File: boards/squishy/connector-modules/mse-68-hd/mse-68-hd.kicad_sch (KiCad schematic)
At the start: 14 parts, among them J1 SCSI PHY Mezz, J2 Conn_02x25_Odd_Even, J3 Conn_01x04, J4 Conn_02x34_Clockwise_Shield, J5 Conn_02x24_Clockwise_Shield, U1 M24C02-RMC

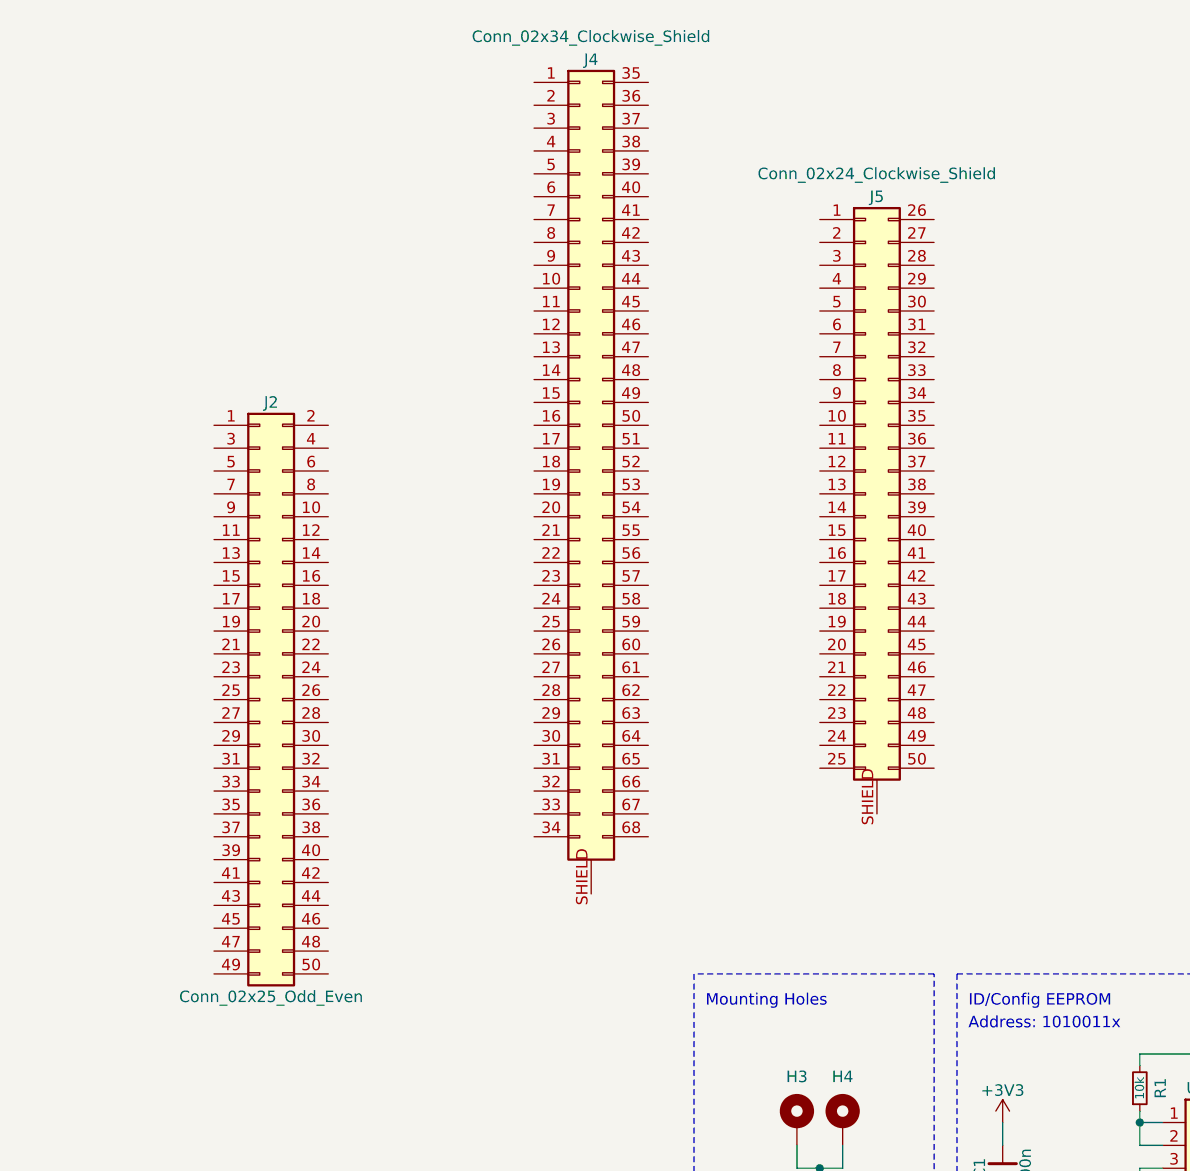
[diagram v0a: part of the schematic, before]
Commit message: squishy: connectors: Removed unneeded connector symbols in the given kicad schematics
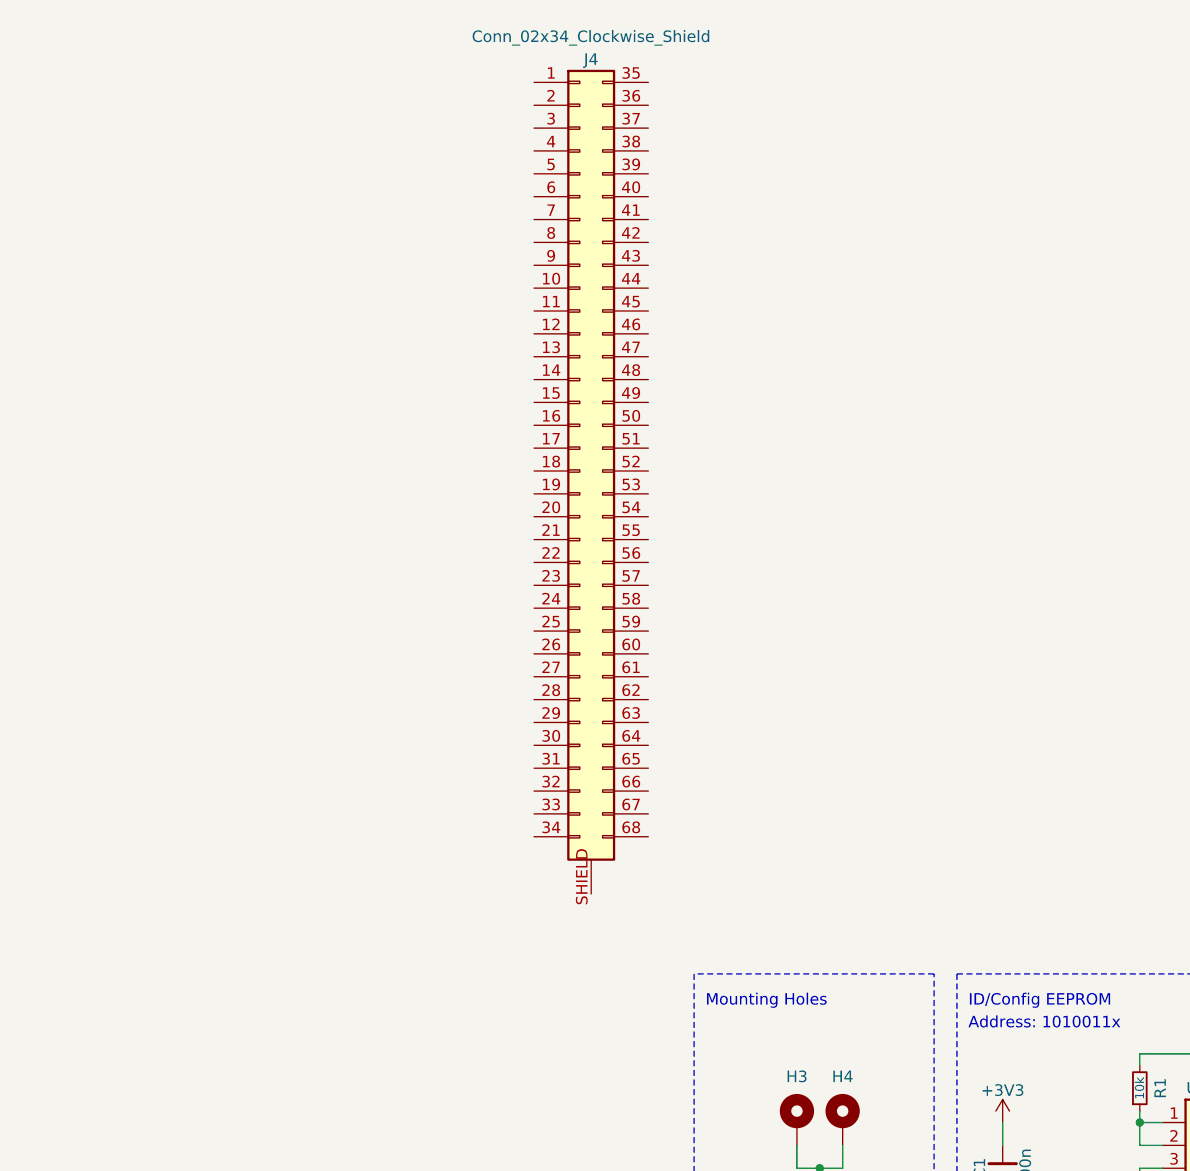
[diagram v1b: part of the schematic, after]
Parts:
- removed J2: Conn_02x25_Odd_Even, Connector_IDC:IDC-Header_2x25_P2.54mm_Horizontal, symbol Connector_Generic:Conn_02x25_Odd_Even
- removed J5: Conn_02x24_Clockwise_Shield, symbol lethalbit-connectors:Conn_02x25_Counter_Clockwise

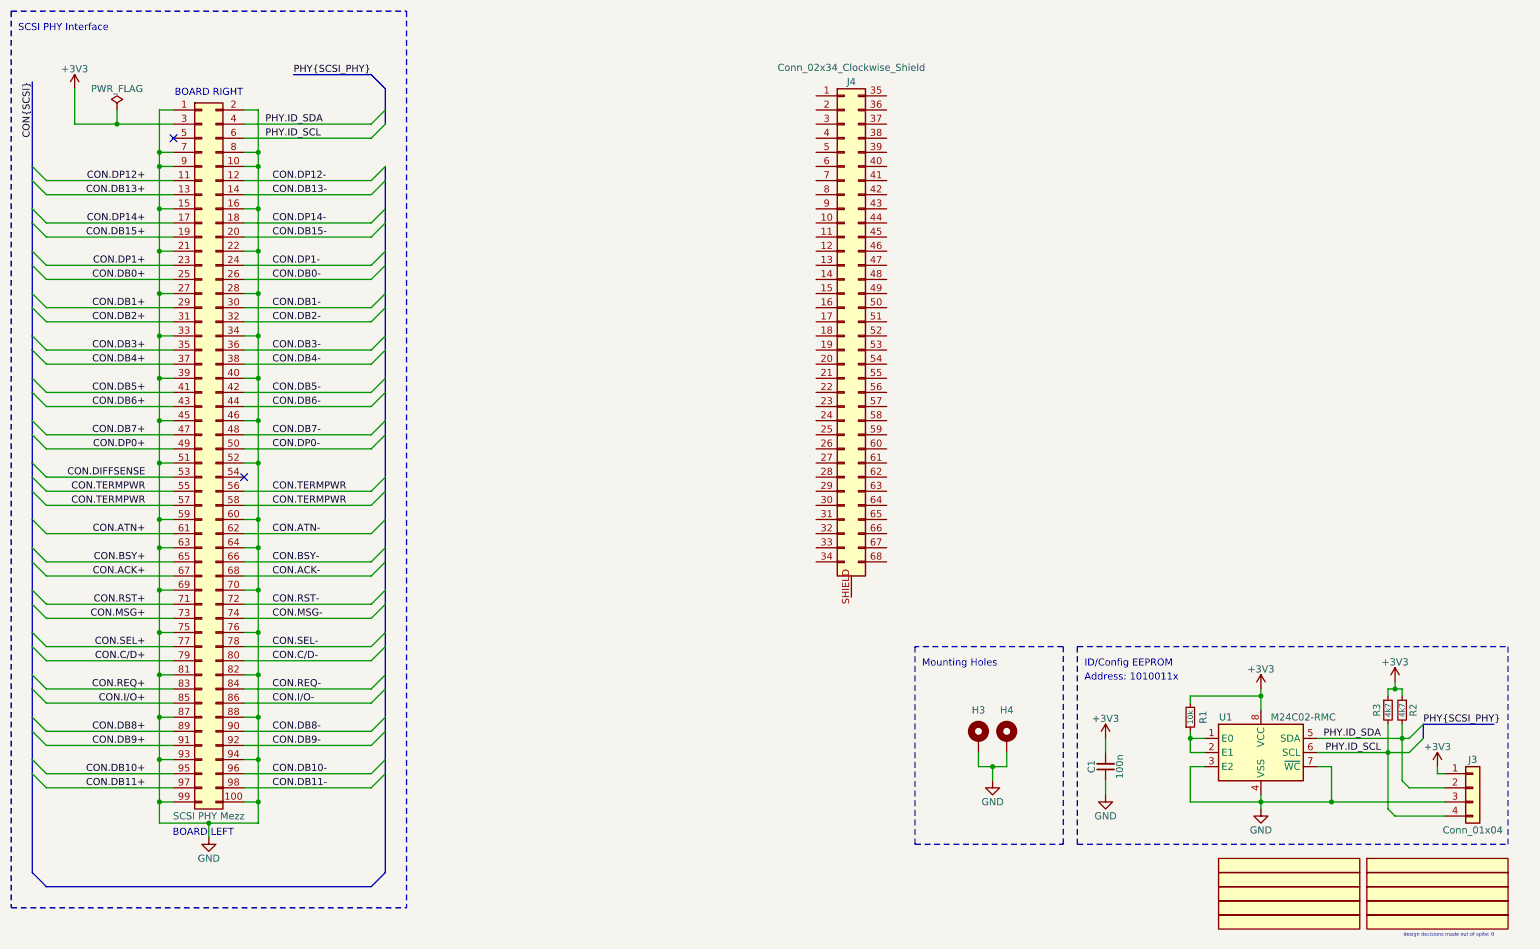
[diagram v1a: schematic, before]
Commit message: squishy: connectors: Built the connector pinout for the 68-pin HD LVD/MSE/SE connector board
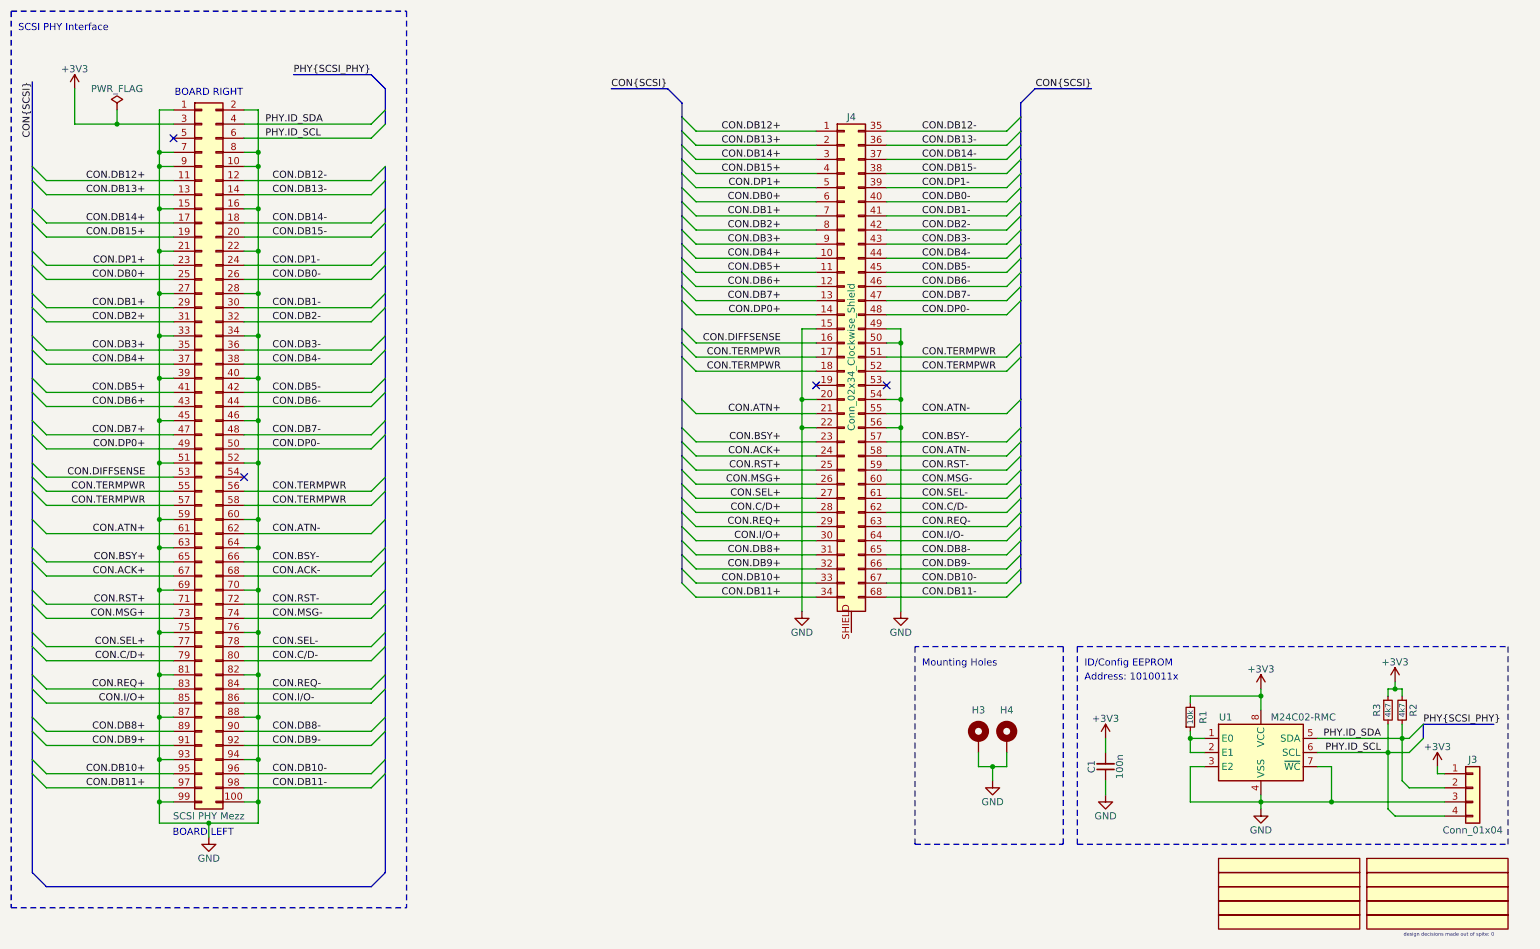
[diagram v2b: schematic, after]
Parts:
- J4: footprint (none) -> lethalbit-connectors:5787082-7
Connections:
- net CON.DP12+ is gone; now on net CON.DB12+: J1.11 (Pin_11)
- net CON.DP12- is gone; now on net CON.DB12-: J1.12 (Pin_12)
- net CON.DP14+ is gone; now on net CON.DB14+: J1.17 (Pin_17)
- net CON.DP14- is gone; now on net CON.DB14-: J1.18 (Pin_18)
- net CON.ACK+: now also J4.24 (Pin_24)
- net CON.ATN+: now also J4.21 (Pin_21)
- net CON.ATN-: now also J4.55 (Pin_55), J4.58 (Pin_58)
- net CON.BSY+: now also J4.23 (Pin_23)
- net CON.BSY-: now also J4.57 (Pin_57)
- net CON.C/D+: now also J4.28 (Pin_28)
- net CON.C/D-: now also J4.62 (Pin_62)
- net CON.DB0+: now also J4.6 (Pin_6)
- net CON.DB0-: now also J4.40 (Pin_40)
- net CON.DB1+: now also J4.7 (Pin_7)
- net CON.DB1-: now also J4.41 (Pin_41)
- net CON.DB10+: now also J4.33 (Pin_33)
- net CON.DB10-: now also J4.67 (Pin_67)
- net CON.DB11+: now also J4.34 (Pin_34)
- net CON.DB11-: now also J4.68 (Pin_68)
- net CON.DB13+: now also J4.2 (Pin_2)
- net CON.DB13-: now also J4.36 (Pin_36)
- net CON.DB15+: now also J4.4 (Pin_4)
- net CON.DB15-: now also J4.38 (Pin_38)
- net CON.DB2+: now also J4.8 (Pin_8)
- net CON.DB2-: now also J4.42 (Pin_42)
- net CON.DB3+: now also J4.9 (Pin_9)
- net CON.DB3-: now also J4.43 (Pin_43)
- net CON.DB4+: now also J4.10 (Pin_10)
- net CON.DB4-: now also J4.44 (Pin_44)
- net CON.DB5+: now also J4.11 (Pin_11)
- net CON.DB5-: now also J4.45 (Pin_45)
- net CON.DB6+: now also J4.12 (Pin_12)
- net CON.DB6-: now also J4.46 (Pin_46)
- net CON.DB7+: now also J4.13 (Pin_13)
- net CON.DB7-: now also J4.47 (Pin_47)
- net CON.DB8+: now also J4.31 (Pin_31)
- net CON.DB8-: now also J4.65 (Pin_65)
- net CON.DB9+: now also J4.32 (Pin_32)
- net CON.DB9-: now also J4.66 (Pin_66)
- net CON.DIFFSENSE: now also J4.16 (Pin_16)
- net CON.DP0+: now also J4.14 (Pin_14)
- net CON.DP0-: now also J4.48 (Pin_48)
- net CON.DP1+: now also J4.5 (Pin_5)
- net CON.DP1-: now also J4.39 (Pin_39)
- net CON.I/O+: now also J4.30 (Pin_30)
- net CON.I/O-: now also J4.64 (Pin_64)
- net CON.MSG+: now also J4.26 (Pin_26)
- net CON.MSG-: now also J4.60 (Pin_60)
- net CON.REQ+: now also J4.29 (Pin_29)
- net CON.REQ-: now also J4.63 (Pin_63)
- net CON.RST+: now also J4.25 (Pin_25)
- net CON.RST-: now also J4.59 (Pin_59)
- net CON.SEL+: now also J4.27 (Pin_27)
- net CON.SEL-: now also J4.61 (Pin_61)
- net CON.TERMPWR: now also J4.17 (Pin_17), J4.18 (Pin_18), J4.51 (Pin_51), J4.52 (Pin_52)
- net GND: now also J4.15 (Pin_15), J4.20 (Pin_20), J4.22 (Pin_22), J4.49 (Pin_49), J4.50 (Pin_50), J4.54 (Pin_54), J4.56 (Pin_56)
- net CON.DB12+: now reaches J4.1 (Pin_1)
- net CON.DB14+: now reaches J4.3 (Pin_3)
- net CON.DB12-: now reaches J4.35 (Pin_35)
- net CON.DB14-: now reaches J4.37 (Pin_37)
- no-connect marks 2 -> 4
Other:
- moved on the sheet: J4

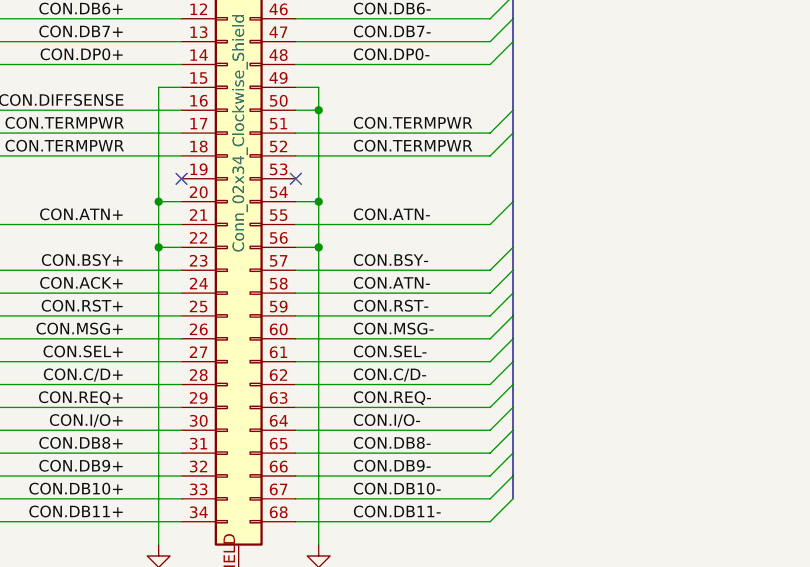
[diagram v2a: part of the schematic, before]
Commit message: squishy: connectors: Routed out the first half of the HVD/LVD/SE 68-pin connector module
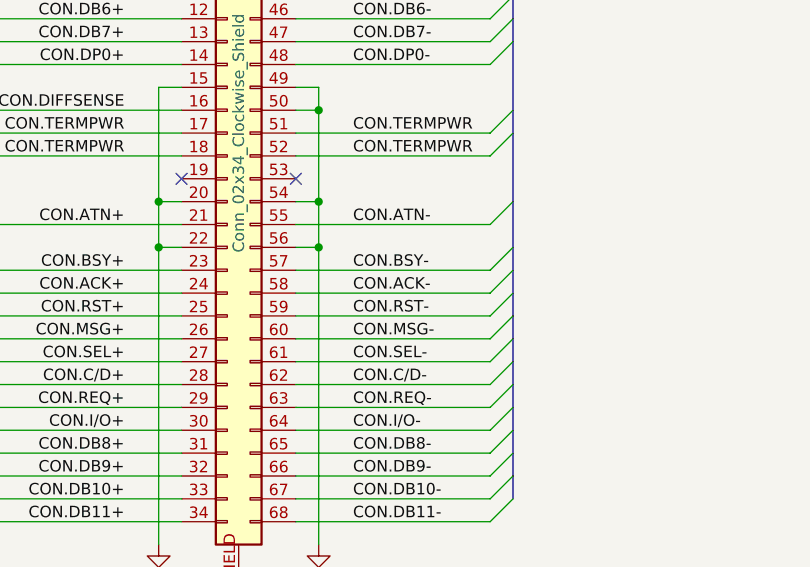
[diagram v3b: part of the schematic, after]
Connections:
- net CON.ACK-: now also J4.58 (Pin_58)
- net CON.ATN-: no longer J4.58 (Pin_58)
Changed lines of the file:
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@@
 		)
 	)
-	(label "CON.ATN-"
+	(label "CON.ACK-"
 		(at 177.8 93.98 0)
 		(effects

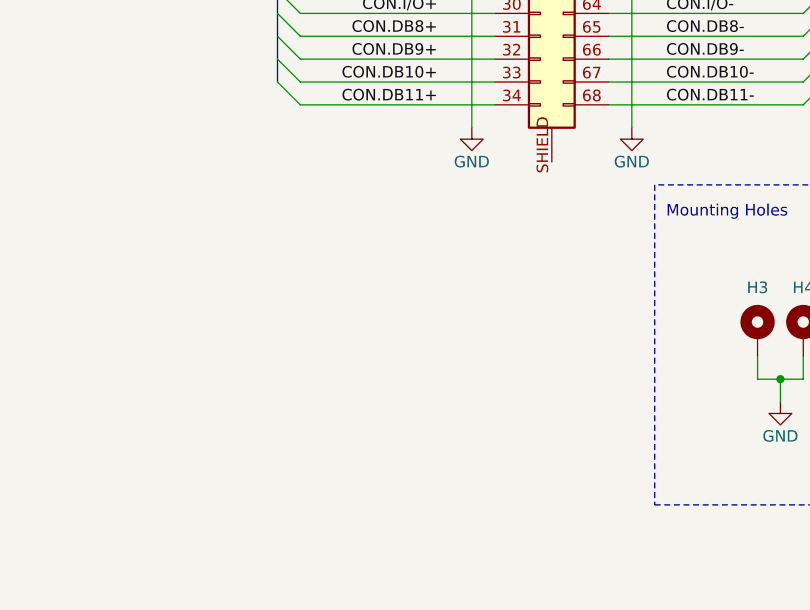
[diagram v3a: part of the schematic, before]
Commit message: squishy: connectors: Completed length matchinig and added sheild handling to the 68-pin HD LVD/MSE/SE connector module
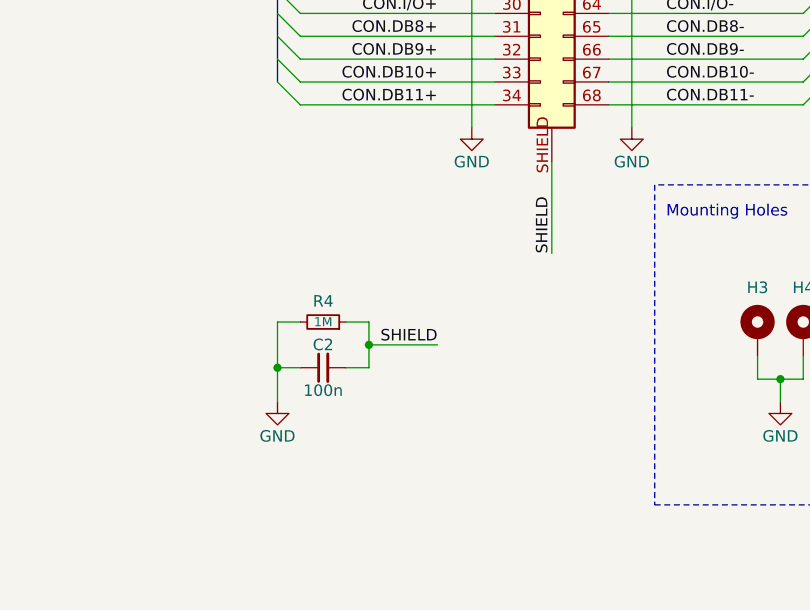
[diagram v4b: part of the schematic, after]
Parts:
- added C2: 100n, rhais_rcl:C0603, symbol Device:C_Small
- added R4: 1M, rhais_rcl:R0603, symbol Device:R_Small
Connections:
- net GND: now also C2.1, R4.2
- net SHIELD: now reaches J4.SHIELD
- net SHIELD: now also C2.2, R4.1
